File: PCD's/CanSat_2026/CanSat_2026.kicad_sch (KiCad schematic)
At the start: 9 parts, among them J1 Conn_01x02_Pin, J2 Conn_01x06, J3 Conn_01x06, J4 9DOF, J5 Conn_01x03_Pin, U1 LM1085-3.3, U2 LP5907MFX-1.8, U3 ESP32-WROOM-32D, U4 SN74AVC4T245PW

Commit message: update to pcb
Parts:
- J2: value Conn_01x06 -> RADIO
- J3: value Conn_01x06 -> BMP280
- J5: value Conn_01x03_Pin -> GPS
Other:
- moved on the sheet: J2
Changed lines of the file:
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@@
 	(wire
 		(pts
-			(xy 172.72 123.19) (xy 172.72 106.68)
-		)
-		(stroke
-			(width 0)
-			(type default)
-		)
-	)
-	(wire
-		(pts
-			(xy 175.26 123.19) (xy 175.26 104.14)
+			(xy 172.72 130.81) (xy 172.72 106.68)
+		)
+		(stroke
+			(width 0)
+			(type default)
+		)
+	)
+	(wire
+		(pts
+			(xy 175.26 130.81) (xy 175.26 104.14)
 		)
 		(stroke
@@
 	(wire
 		(pts
+			(xy 170.18 130.81) (xy 170.18 123.19)
+		)
+		(stroke
+			(width 0)
+			(type default)
+		)
+	)
+	(wire
+		(pts
 			(xy 160.02 107.95) (xy 144.78 107.95)
 		)
@@
 		(pts
 			(xy 172.72 106.68) (xy 149.86 106.68)
+		)
+		(stroke
+			(width 0)
+			(type default)
+		)
+	)
+	(wire
+		(pts
+			(xy 182.88 130.81) (xy 182.88 123.19)
 		)
 		(stroke
@@
 			)
 		)
-		(property "Value" "Conn_01x03_Pin"
+		(property "Value" "GPS"
 			(at 204.47 132.08 90)
 			(effects
@@
 			)
 		)
-		(property "Value" "Conn_01x06"
+		(property "Value" "BMP280"
 			(at 158.75 132.08 90)
 			(effects
@@
 	(symbol
 		(lib_id "Connector_Generic:Conn_01x06")
-		(at 177.8 128.27 270)
+		(at 177.8 135.89 270)
 		(unit 1)
 		(exclude_from_sim no)
@@
 		(dnp no)
 		(property "Reference" "J2"
-			(at 163.83 128.27 0)
-			(effects
-				(font
-					(size 1.27 1.27)
-				)
-			)
-		)
-		(property "Value" "Conn_01x06"
-			(at 166.37 128.27 0)
+			(at 163.83 135.89 0)
+			(effects
+				(font
+					(size 1.27 1.27)
+				)
+			)
+		)
+		(property "Value" "RADIO"
+			(at 166.37 135.89 0)
 			(effects
 				(font
@@
 		)
 		(property "Footprint" "Connector_JST:JST_GH_SM06B-GHS-TB_1x06-1MP_P1.25mm_Horizontal"
-			(at 177.8 128.27 0)
+			(at 177.8 135.89 0)
 			(effects
 				(font
@@
 		)
 		(property "Datasheet" "~"
-			(at 177.8 128.27 0)
+			(at 177.8 135.89 0)
 			(effects
 				(font
@@
 		)
 		(property "Description" "Generic connector, single row, 01x06, script generated (kicad-library-utils/schlib/autogen/connector/)"
-			(at 177.8 128.27 0)
-			(effects
-				(font
+			(at 177.8 135.89 0)
+			(effects
+				(font

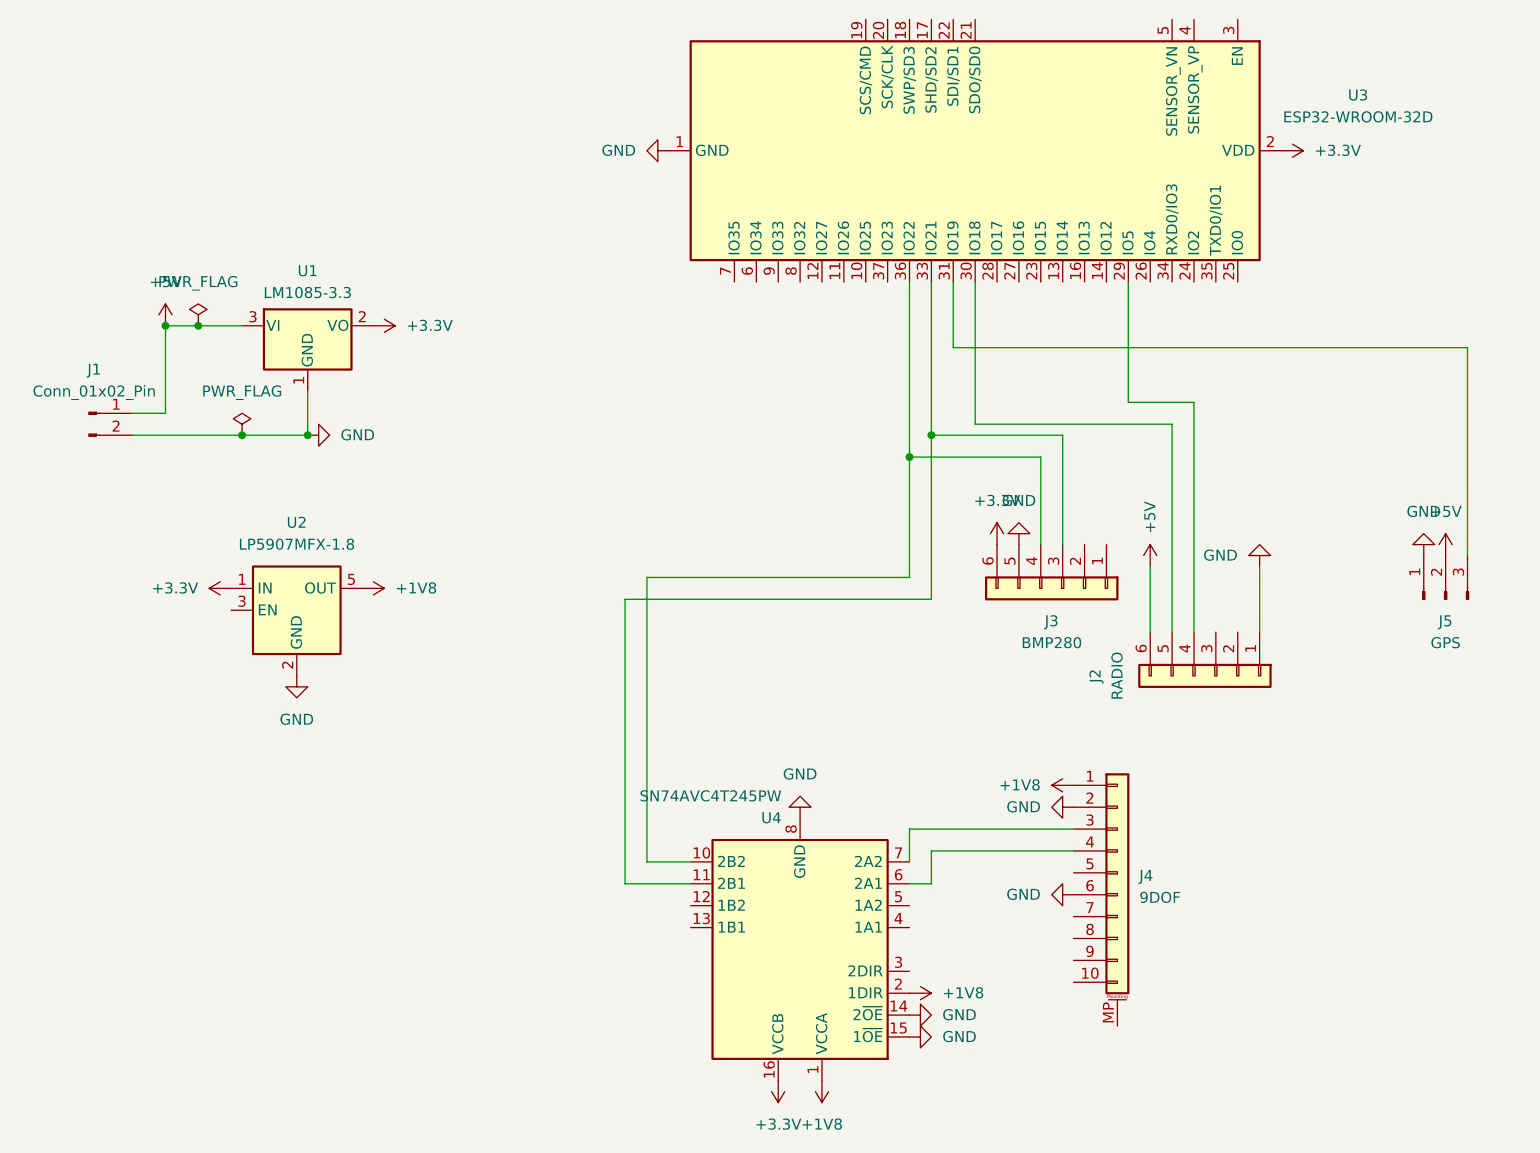
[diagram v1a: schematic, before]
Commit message: Fix pcb for merge compatibility
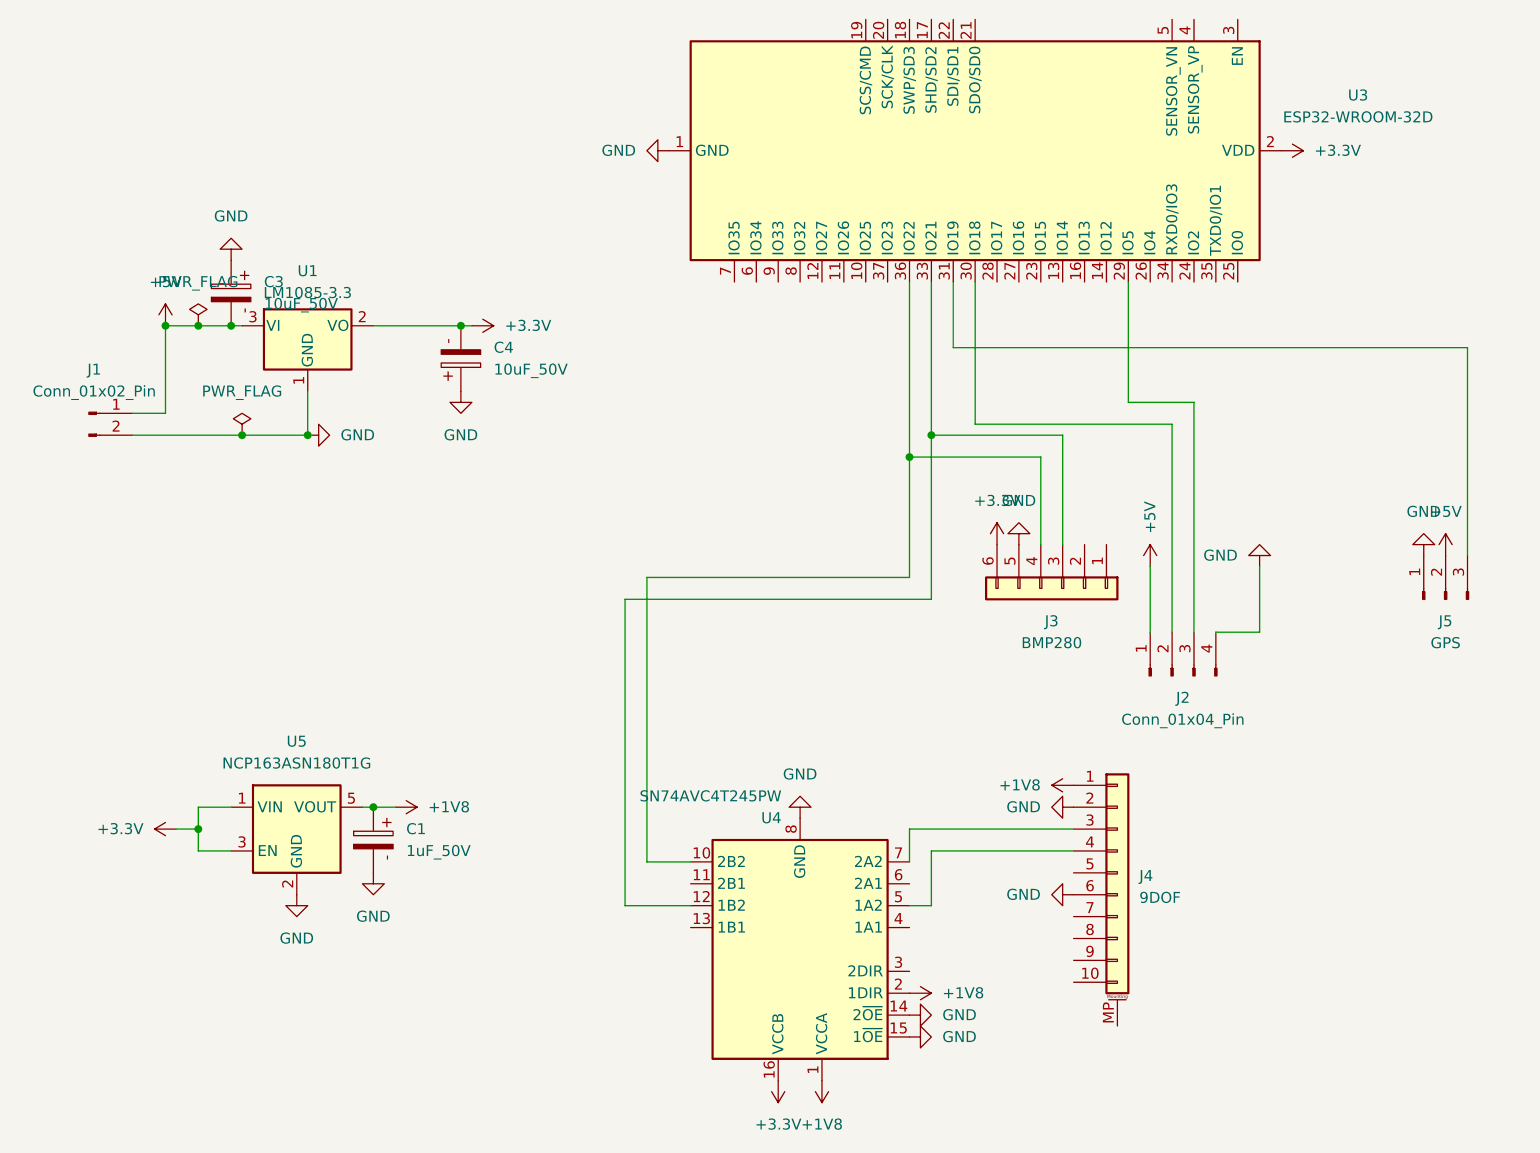
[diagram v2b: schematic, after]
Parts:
- removed J2: RADIO, Connector_JST:JST_GH_SM06B-GHS-TB_1x06-1MP_P1.25mm_Horizontal, symbol Connector_Generic:Conn_01x06
- removed U2: LP5907MFX-1.8, Package_TO_SOT_SMD:SOT-23-5_HandSoldering, symbol Regulator_Linear:LP5907MFX-1.8
- added C1: 1uF_50V, Capacitor_THT:C_Disc_D5.0mm_W2.5mm_P5.00mm, symbol PCM_SL_Capacitors:1uF_50V
- added C3, C4: 10uF_50V, Capacitor_THT:C_Radial_D6.3mm_H11.0mm_P2.50mm, symbol PCM_SL_Capacitors:10uF_50V
- added J2: Conn_01x04_Pin, Connector_PinHeader_2.54mm:PinHeader_1x04_P2.54mm_Vertical, symbol Connector:Conn_01x04_Pin
- added U5: NCP163ASN180T1G, Package_SO:TSOP-5_1.65x3.05mm_P0.95mm, symbol Regulator_Linear:NCP163ASN180T1G
- U1: footprint Package_TO_SOT_THT:TO-220-3_Horizontal_TabUp -> Package_TO_SOT_THT:TO-220-3_Vertical
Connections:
- net +1V8: now also C1.1, U5.5 (VOUT)
- net +3.3V: now also C4.2, U5.1 (VIN), U5.3 (EN)
- net +5V: now also C3.2, J2.1 (Pin_1)
- net GND: now also C1.2, C3.1, C4.1, J2.4 (Pin_4), U5.2 (GND)
- net at J3.3 (Pin_3), U3.33 (IO21): now also U4.12 (1B2); no longer U4.11 (2B1)
- net at U4.5 (1A2): now also J4.4 (Pin_4)
- net at U4.6 (2A1): no longer J4.4 (Pin_4)
- net at U3.29 (IO5): now also J2.3 (Pin_3)
- net at U3.30 (IO18): now also J2.2 (Pin_2)
